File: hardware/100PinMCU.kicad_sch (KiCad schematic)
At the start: 28 parts, among them J1 SWD_Header_02x02, U2 STM32G491VET6_1, Y1 Crystal

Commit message: labeled + stm32 cube layout
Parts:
- renumbered C1 to C17, C2 to C18, C14 to C19, C3 to C20, C9 to C21, C4 to C22, C10 to C23, C5 to C24, C12 to C25, C6 to C26, C13 to C27, C7 to C28, C8 to C29, C11 to C30, D2 to D3, D1 to D4, FB2 to FB1, FB1 to FB2, J1 to J2, R4 to R10, R5 to R11, R1 to R12, R3 to R13, R2 to R14, U2 to U3

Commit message: added debug led
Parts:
- renumbered D3 to D10, D4 to D11, R10 to R17, R11 to R18, R12 to R19, R13 to R20, R14 to R21
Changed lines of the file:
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@@
 		(dnp no)
 		(fields_autoplaced yes)
-		(property "Reference" "R12"
+		(property "Reference" "R19"
 			(at 182.245 105.4099 0)
 			(effects
@@
 			(project "PS-100PinMCU"
 				(path "/2365a867-6254-4a7c-9718-f325e0bbac5c/f0812fe3-6145-4dbc-9ba0-df8905216d8c"
-					(reference "R12")
+					(reference "R19")
 					(unit 1)
 				)
@@
 		(dnp no)
 		(fields_autoplaced yes)
-		(property "Reference" "R14"
+		(property "Reference" "R21"
 			(at 234.95 114.9349 0)
 			(effects
@@
 			(project "PS-100PinMCU"
 				(path "/2365a867-6254-4a7c-9718-f325e0bbac5c/f0812fe3-6145-4dbc-9ba0-df8905216d8c"
-					(reference "R14")
+					(reference "R21")
 					(unit 1)
 				)
@@
 		(dnp no)
 		(fields_autoplaced yes)
-		(property "Reference" "R10"
+		(property "Reference" "R17"
 			(at 138.43 21.59 90)
 			(effects
@@
 			(project ""
 				(path "/2365a867-6254-4a7c-9718-f325e0bbac5c/f0812fe3-6145-4dbc-9ba0-df8905216d8c"
-					(reference "R10")
+					(reference "R17")
 					(unit 1)
 				)
@@
 		(on_board yes)
 		(dnp no)
-		(property "Reference" "R11"
+		(property "Reference" "R18"
 			(at 138.43 33.02 90)
 			(effects
@@
 			(project ""
 				(path "/2365a867-6254-4a7c-9718-f325e0bbac5c/f0812fe3-6145-4dbc-9ba0-df8905216d8c"
-					(reference "R11")
+					(reference "R18")
 					(unit 1)
 				)
@@
 		(on_board yes)
 		(dnp no)
-		(property "Reference" "R13"
+		(property "Reference" "R20"
 			(at 225.806 94.996 90)
 			(effects
@@
 			(project "PS-100PinMCU"
 				(path "/2365a867-6254-4a7c-9718-f325e0bbac5c/f0812fe3-6145-4dbc-9ba0-df8905216d8c"
-					(reference "R13")
+					(reference "R20")
 					(unit 1)
 				)
@@
 		(dnp no)
 		(fields_autoplaced yes)
-		(property "Reference" "D4"
+		(property "Reference" "D11"
 			(at 247.015 109.2199 90)
 			(effects
@@
 			(project "PS-100PinMCU"
 				(path "/2365a867-6254-4a7c-9718-f325e0bbac5c/f0812fe3-6145-4dbc-9ba0-df8905216d8c"
-					(reference "D4")
+					(reference "D11")
 					(unit 1)
 				)
@@
 		(dnp no)
 		(fields_autoplaced yes)
-		(property "Reference" "D3"
+		(property "Reference" "D10"
 			(at 236.22 105.0924 90)
 			(effects
@@
 			(project "PS-100PinMCU"
 				(path "/2365a867-6254-4a7c-9718-f325e0bbac5c/f0812fe3-6145-4dbc-9ba0-df8905216d8c"
-					(reference "D3")
-					(unit 1)
-				)
+					(reference "D10")
+					(unit 1)
+				)

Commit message: added calcs, cleaned up, addressed comments
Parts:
- removed C17, C18: 26p, Capacitor_SMD:C_0603_1608Metric_Pad1.08x0.95mm_HandSolder, symbol Device:C
- removed D10: LED, LED_SMD:LED_0201_0603Metric, symbol Device:LED
- removed D11: D_TVS, Diode_SMD:D_SOD-323, symbol Device:D_TVS
- removed R17, R18: 22, Resistor_SMD:R_0603_1608Metric_Pad0.98x0.95mm_HandSolder, symbol Device:R_US
- removed R20: 10k, Resistor_SMD:R_0603_1608Metric_Pad0.98x0.95mm_HandSolder, symbol Device:R_US
- removed R21: 1k, Resistor_SMD:R_0603_1608Metric_Pad0.98x0.95mm_HandSolder, symbol Device:R_US
- removed S1: 450406020024, LHRS_Special:BootSW, symbol Switch:SW_SPDT
- removed U3: STM32G491VET6_1, LHRS_ICs:LQFP_491VET6_STM, symbol lhrs_ics:STM32G491VET6_1
- added C8, C9: 26p, Capacitor_SMD:C_0603_1608Metric_Pad1.08x0.95mm_HandSolder, symbol Device:C
- added D10: LED, LED_SMD:LED_0603_1608Metric, symbol lhrs_misc:Blue_LED
- added D8: TVS, Diode_SMD:D_SOD-323, symbol lhrs_misc:Boot_TVS
- added D9: RGB_LED, LHRS_Special:RGB_LED, symbol lhrs_special:RGB_LED
- added J6: SWD, Connector_PinHeader_2.54mm:PinHeader_1x04_P2.54mm_Vertical, symbol Connector_Generic:Conn_01x04
- added R14, R15: 22, Resistor_SMD:R_0603_1608Metric_Pad0.98x0.95mm_HandSolder, symbol Device:R
- added R16, R17, R18, R20: 1k, Resistor_SMD:R_0603_1608Metric_Pad0.98x0.95mm_HandSolder, symbol Device:R
- added R19: 10k, Resistor_SMD:R_0603_1608Metric_Pad0.98x0.95mm_HandSolder, symbol Device:R
- added SW1: SW_SPDT, LHRS_Special:BootSW, symbol Switch:SW_SPDT
- added U2: STM32G473VETx, LHRS_Special:100PinMCU, symbol lhrs_special:STM32G473VET6
- C10: renamed from C20; value 10uF -> 10u
- C11: renamed from C21; value 0.1uF -> 0.1u
- C12: renamed from C22; value 0.1uF -> 0.1u
- C13: renamed from C23; value 0.1uF -> 0.1u
- C14: renamed from C19; value 0.1uF -> 0.1u
- C15: renamed from C24; value 0.1uF -> 0.1u
- C16: renamed from C25; value 1uF -> 1u
- C17: renamed from C26; value 0.1uF -> 0.1u
- C18: renamed from C27; value 1uF -> 1u
- C19: renamed from C28; value 0.1uF -> 0.1u
- C20: renamed from C29; value 0.1uF -> 0.1u
- C21: renamed from C30; value 0.1uF -> 0.1u
- J5: renamed from J2; value SWD_Header_02x02 -> SWD_Header
- R13: renamed from R19; symbol Device:R_US -> Device:R
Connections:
- net GND: now also FB1.2, C8.1, C9.1, D8.1 (A1), J6.2 (Pin_2), R16.2, R17.2, R18.2, R20.2, SW1.3 (C), U2.23 (VSS), U2.48 (VSS), U2.63 (VSS), U2.74 (VSS), U2.99 (VSS); no longer FB1.1
- net GNDA: now also FB1.1, U2.35 (VSSA); no longer FB1.2
- net PA0: now also D9.5, U2.20 (PA0-GPIO_BLUE)
- net PA1: now also D9.3, U2.21 (PA1-GPIO_RED)
- net PA10: now also U2.71 (PA10)
- net PA15: now also U2.78 (PA15)
- net PA2: now also D9.1, U2.22 (PA2-GPIO_GREEN)
- net PA3: now also U2.25 (PA3)
- net PA4: now also U2.26 (PA4)
- net PA5: now also U2.27 (PA5)
- net PA6: now also U2.28 (PA6)
- net PA7: now also U2.29 (PA7)
- net PA8: now also U2.69 (PA8)
- net PA9: now also U2.70 (PA9)
- net PB0: now also U2.32 (PB0)
- net PB1: now also U2.33 (PB1)
- net PB10: now also U2.47 (PB10)
- net PB11: now also U2.50 (PB11)
- net PB12: now also U2.51 (PB12)
- net PB13: now also U2.52 (PB13)
- net PB14: now also U2.53 (PB14)
- net PB15: now also U2.54 (PB15)
- net PB2: now also U2.34 (PB2)
- net PB3: now also U2.90 (PB3)
- net PB4: now also U2.91 (PB4)
- net PB5: now also U2.92 (PB5)
- net PB6: now also U2.93 (PB6)
- net PB7: now also U2.94 (PB7)
- net PB9: now also U2.96 (PB9)
- net PC0: now also U2.15 (PC0)
- net PC1: now also U2.16 (PC1)
- net PC10: now also U2.79 (PC10)
- net PC11: now also U2.80 (PC11)
- net PC12: now also U2.81 (PC12)
- net PC2: now also U2.17 (PC2)
- net PC3: now also U2.18 (PC3)
- net PC4: now also U2.30 (PC4)
- net PC5: now also U2.31 (PC5)
- net PC6: now also U2.65 (PC6)
- net PC7: now also U2.66 (PC7)
- net PC8: now also U2.67 (PC8)
- net PC9: now also U2.68 (PC9)
- net PD0: now also U2.82 (PD0)
- net PD1: now also U2.83 (PD1)
- net PD10: now also U2.57 (PD10)
- net PD11: now also U2.58 (PD11)
- net PD12: now also U2.59 (PD12)
- net PD13: now also U2.60 (PD13)
- net PD14: now also U2.61 (PD14)
- net PD15: now also U2.62 (PD15)
- net PD2: now also U2.84 (PD2)
- net PD3: now also U2.85 (PD3)
- net PD4: now also U2.86 (PD4)
- net PD5: now also U2.87 (PD5)
- net PD6: now also U2.88 (PD6)
- net PD7: now also U2.89 (PD7)
- net PD8: now also U2.55 (PD8)
- net PD9: now also U2.56 (PD9)
- net PE0: now also U2.97 (PE0)
- net PE1: now also U2.98 (PE1)
- net PE11: now also U2.42 (PE11)
- net PE12: now also U2.43 (PE12)
- net PE13: now also U2.44 (PE13)
- net PE14: now also U2.45 (PE14)
- net PE15: now also U2.46 (PE15)
- net PE2: now also U2.1 (PE2)
- net PE3: now also U2.2 (PE3)
- net PE4: now also U2.3 (PE4)
- net PE5: now also U2.4 (PE5)
- net PE6: now also U2.5 (PE6)
- net PE7: now also U2.38 (PE7)
- net PE8: now also U2.39 (PE8)
- net PE9: now also U2.40 (PE9)
- net PF10: now also U2.11 (PF10)
- net PF2: now also U2.19 (PF2)
- net PF9: now also U2.10 (PF9)
- net SWCLK: now also R14.1, U2.77 (PA14)
- net SWDIO: now also R15.1, U2.76 (PA13)
- net USB_DM: now also U2.72 (PA11)
- net USB_DP: now also U2.73 (PA12)
- net VDDA: now also U2.36 (VREF+), U2.37 (VDDA)
- net at Y1.1: now also C9.2, U2.13 (PF1-OSC_OUT)
- net at Y1.2: now also C8.2, U2.12 (PF0-OSC_IN)
- net at J5.3 (Pin_3): now also J6.3 (Pin_3), R14.2
- net at J5.4 (Pin_4): now also J6.4 (Pin_4), R15.2
- net 3V3 renamed +3V3
- net +3V3: now also J6.1 (Pin_1), SW1.1 (A), U2.100 (VDD), U2.24 (VDD), U2.49 (VDD), U2.6 (VBAT), U2.64 (VDD), U2.75 (VDD)
- net PG10-NRST renamed NRST
- net NRST: now also U2.14 (PG10-NRST)
- new net: D10.1 (K), R20.1
- new net: D10.2 (A), D8.2 (A2), R19.2, SW1.2 (B)
- new net: D9.2, R16.1
- new net: D9.4, R17.1
- new net: D9.6, R18.1
- new net BOOT0: R19.1, U2.95 (PB8-BOOT0)
- new net PC13: U2.7 (PC13)
- new net PC14: U2.8 (PC14-OSC32_IN)
- new net PC15: U2.9 (PC15-OSC32_OUT)
- new net PE10: U2.41 (PE10)
- no-connect marks 3 -> 0
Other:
- note added: "*Place oscillator circuitry close to MCU"
- note added: "100 Pin MCU"
- note added: "BLUE"
- note added: "BOOT0 low -> Load into app BOOT0 high -> Load into bootloader"
- note added: "Beware, using PC13 - 15 as GPIOs ..."
- note added: "CLK"
- note added: "Conn"
- note added: "GREEN"
- note added: "IO"
- note added: "Main Flash (user code)"
- note added: "Pin Headers"
- note added: "Place these decoupling caps as close as possible to their respective leads."
- note added: "Power Source Filtering/Isolation"
- note added: "RED"
- note added: "RGB LED"
- note added: "Reset BTN + Boot SW"
- note added: "Serial Wire Communication"
- note added: "Sys Memory (bootloader)"
- note added: "Use PA0, PA1, PA2 to PWM RGB LED (TIM2_CH1, TIM2_CH2, TIM2_CH3)"
- note removed: "BOOT = 0 (Logic LOW) Mode: Main Flash Memory. BOOT = 1 (Logic HIGH) Mode: System Memory."
- note removed: "Boot Switch"
- note removed: "Buttons & Stuff (External Reset)"
- note removed: "Bypass/Separation"
- note removed: "C1 = C2 = 2x(CL-CStray) C1 = C2 = 2x(18p-5p) C1 = C2 = 26p"
- note removed: "Place immediately adjacent to OSC_IN/OUT."
- note removed: "Reset"
- note removed: "System"
- note removed: "User"
- moved on the sheet: C10, C11, C12, C13, C14, C15, C16, C17, C18, C19, C20, C21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

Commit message: fixed ERC warnings
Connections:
- net +3V3 renamed +3v3

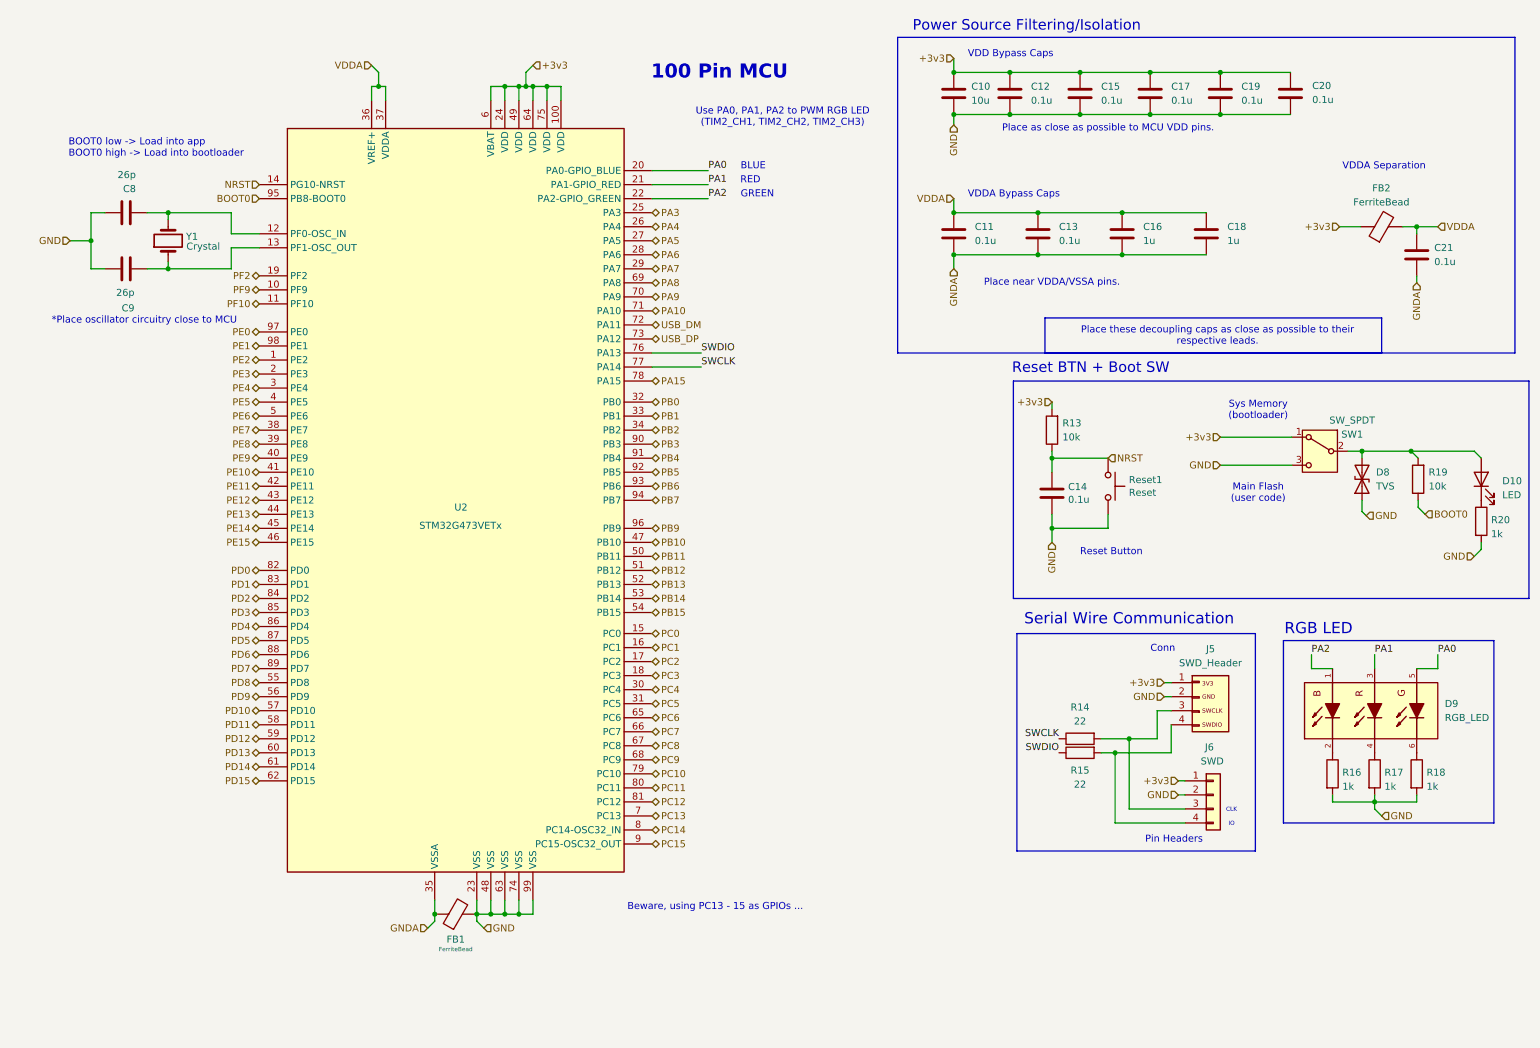
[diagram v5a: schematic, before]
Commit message: added pin layout ss, resolved erc errors, added p/n
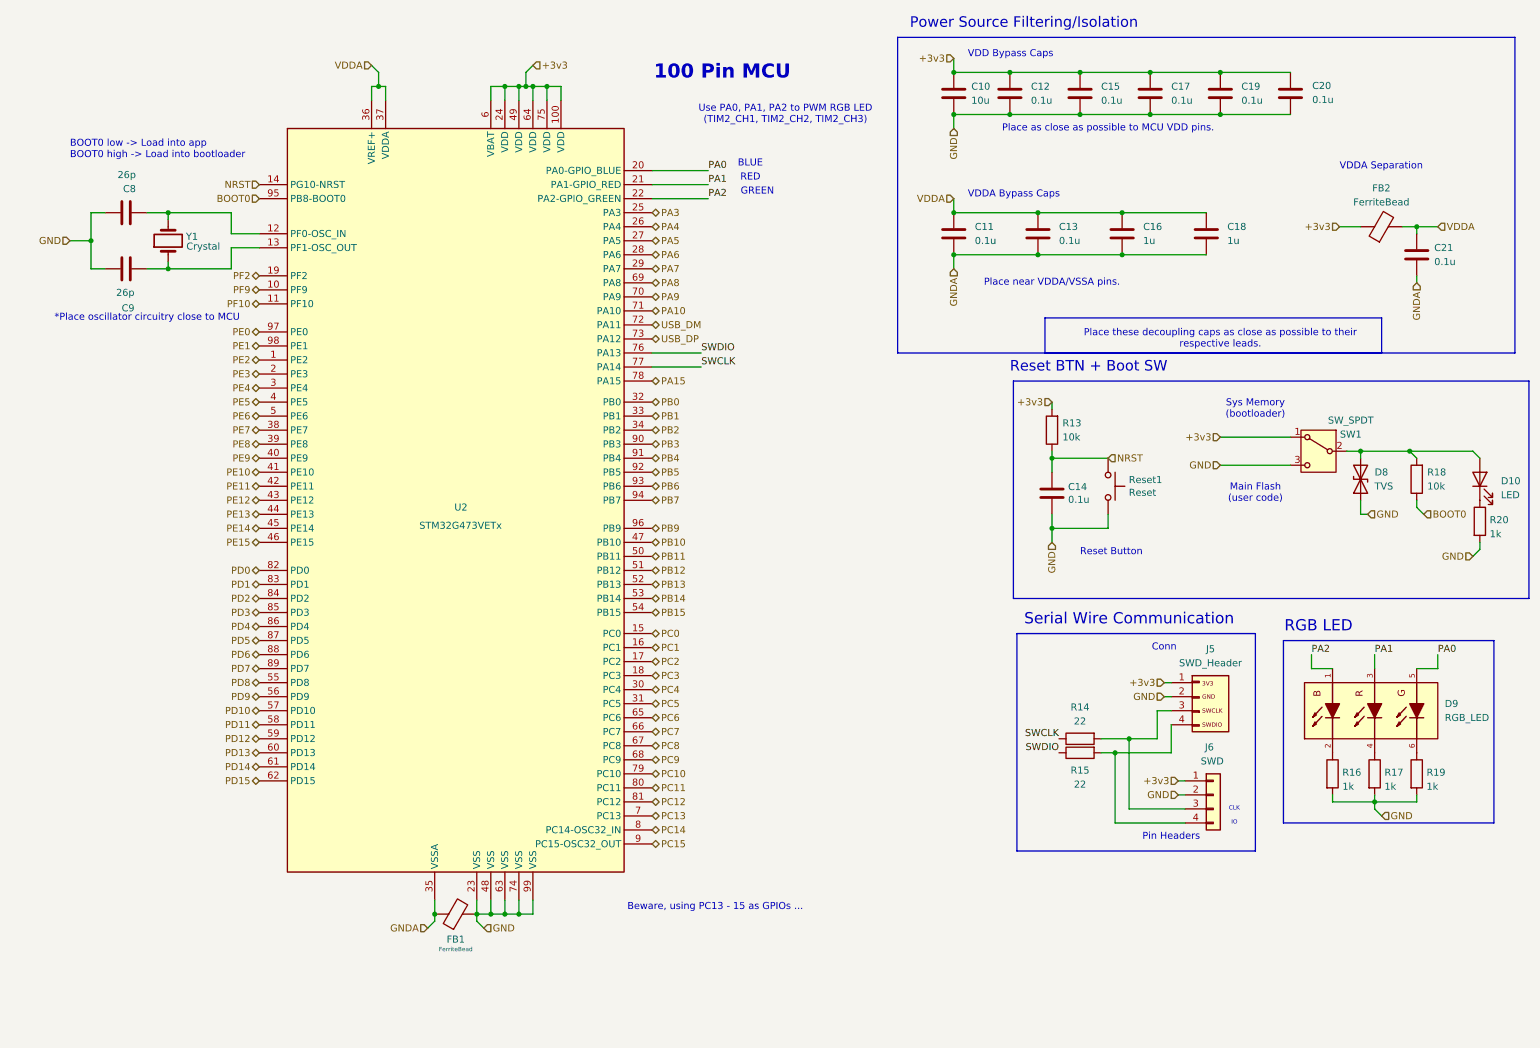
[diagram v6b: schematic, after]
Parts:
- renumbered R19 to R18, R18 to R19
